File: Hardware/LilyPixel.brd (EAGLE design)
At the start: 20 x 20 mm, 11 parts, among them U1 WS2811

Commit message: Update to v10 for release
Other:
- board text added: "v10"
- board text removed: "v01"
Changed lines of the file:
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@@
 <layer number="41" name="tRestrict" color="4" fill="10" visible="no" active="yes"/>
 <layer number="42" name="bRestrict" color="1" fill="10" visible="no" active="yes"/>
+<layer number="43" name="vRestrict" color="2" fill="10" visible="no" active="yes"/>
 <layer number="44" name="Drills" color="7" fill="1" visible="no" active="yes"/>
 <layer number="45" name="Holes" color="7" fill="1" visible="yes" active="yes"/>
@@
 <layer number="37" name="tTest" color="7" fill="1" visible="no" active="no"/>
 <layer number="38" name="bTest" color="7" fill="1" visible="no" active="no"/>
-<layer number="43" name="vRestrict" color="2" fill="10" visible="no" active="no"/>
 <layer number="47" name="Measures" color="7" fill="1" visible="no" active="no"/>
 <layer number="48" name="Document" color="7" fill="1" visible="no" active="no"/>
@@
 <polygon width="0.2032" layer="29">
 <vertex x="-6" y="0"/>
-<vertex x="-11" y="0"/>
-<vertex x="-11" y="11"/>
-<vertex x="0" y="11"/>
+<vertex x="-10.111" y="0"/>
+<vertex x="-10.111" y="9.984"/>
+<vertex x="0" y="9.984"/>
 <vertex x="0" y="8.2"/>
 <vertex x="-1.4" y="7.9"/>
@@
 </polygon>
 <polygon width="0.2032" layer="29">
-<vertex x="0" y="11"/>
-<vertex x="11" y="11"/>
-<vertex x="11" y="0"/>
+<vertex x="0" y="9.984"/>
+<vertex x="10.111" y="9.984"/>
+<vertex x="10.111" y="0"/>
 <vertex x="6" y="0"/>
 <vertex x="6.7" y="0.5"/>
@@
 </polygon>
 <polygon width="0.2032" layer="29">
-<vertex x="11" y="0"/>
-<vertex x="11" y="-11"/>
-<vertex x="0" y="-11"/>
+<vertex x="10.111" y="0"/>
+<vertex x="10.111" y="-10.111"/>
+<vertex x="0" y="-10.111"/>
 <vertex x="0" y="-8.1"/>
 <vertex x="1.1" y="-8"/>
@@
 </polygon>
 <polygon width="0.2032" layer="29">
-<vertex x="0" y="-11"/>
-<vertex x="-11" y="-11"/>
-<vertex x="-11" y="0"/>
+<vertex x="0" y="-10.111"/>
+<vertex x="-10.111" y="-10.111"/>
+<vertex x="-10.111" y="0"/>
 <vertex x="-5.9" y="0"/>
 <vertex x="-6.9" y="-0.7"/>
@@
 <polygon width="0.2032" layer="41">
 <vertex x="-6" y="0"/>
-<vertex x="-11" y="0"/>
-<vertex x="-11" y="11"/>
-<vertex x="0" y="11"/>
+<vertex x="-10.111" y="0"/>
+<vertex x="-10.111" y="9.984"/>
+<vertex x="0" y="9.984"/>
 <vertex x="0" y="8.2"/>
 <vertex x="-1.4" y="7.9"/>
@@
 </polygon>
 <polygon width="0.2032" layer="41">
-<vertex x="0" y="11"/>
-<vertex x="11" y="11"/>
-<vertex x="11" y="0"/>
+<vertex x="0" y="9.984"/>
+<vertex x="10.111" y="9.984"/>
+<vertex x="10.111" y="0"/>
 <vertex x="6" y="0"/>
 <vertex x="6.7" y="0.5"/>
@@
 </polygon>
 <polygon width="0.2032" layer="41">
-<vertex x="11" y="0"/>
-<vertex x="11" y="-11"/>
-<vertex x="0" y="-11"/>
+<vertex x="10.111" y="0"/>
+<vertex x="10.111" y="-10.111"/>
+<vertex x="0" y="-10.111"/>
 <vertex x="0" y="-8.1"/>
 <vertex x="1.1" y="-8"/>
@@
 </polygon>
 <polygon width="0.2032" layer="41">
-<vertex x="0" y="-11"/>
-<vertex x="-11" y="-11"/>
-<vertex x="-11" y="0"/>
+<vertex x="0" y="-10.111"/>
+<vertex x="-10.111" y="-10.111"/>
+<vertex x="-10.111" y="0"/>
 <vertex x="-5.9" y="0"/>
 <vertex x="-6.9" y="-0.7"/>
@@
 <polygon width="0.2032" layer="42">
 <vertex x="-6" y="0"/>
-<vertex x="-11" y="0"/>
-<vertex x="-11" y="11"/>
-<vertex x="0" y="11"/>
+<vertex x="-10.111" y="0"/>
+<vertex x="-10.111" y="9.984"/>
+<vertex x="0" y="9.984"/>
 <vertex x="0" y="8.2"/>
 <vertex x="-1.4" y="7.9"/>
@@
 </polygon>
 <polygon width="0.2032" layer="42">
-<vertex x="0" y="11"/>
-<vertex x="11" y="11"/>
-<vertex x="11" y="0"/>
+<vertex x="0" y="9.984"/>
+<vertex x="10.111" y="9.984"/>
+<vertex x="10.111" y="0"/>
 <vertex x="6" y="0"/>
 <vertex x="6.7" y="0.5"/>
@@
 </polygon>
 <polygon width="0.2032" layer="42">
-<vertex x="11" y="0"/>
-<vertex x="11" y="-11"/>
-<vertex x="0" y="-11"/>
+<vertex x="10.111" y="0"/>
+<vertex x="10.111" y="-10.111"/>
+<vertex x="0" y="-10.111"/>
 <vertex x="0" y="-8.1"/>
 <vertex x="1.1" y="-8"/>
@@
 </polygon>
 <polygon width="0.2032" layer="42">
-<vertex x="0" y="-11"/>
-<vertex x="-11" y="-11"/>
-<vertex x="-11" y="0"/>
+<vertex x="0" y="-10.111"/>
+<vertex x="-10.111" y="-10.111"/>
+<vertex x="-10.111" y="0"/>
 <vertex x="-5.9" y="0"/>
 <vertex x="-6.9" y="-0.7"/>
@@
 <text x="3.81" y="1.905" size="0.8128" layer="21" font="vector" ratio="15">DI</text>
 <text x="-4.826" y="-2.667" size="0.8128" layer="21" font="vector" ratio="15">DI</text>
-<text x="-9.271" y="-1.524" size="1.27" layer="16" font="vector" ratio="15" rot="MR90">v01</text>
+<text x="-9.271" y="-1.524" size="1.27" layer="16" font="vector" ratio="15" rot="MR90">v10</text>
 </plain>
 <attributes>

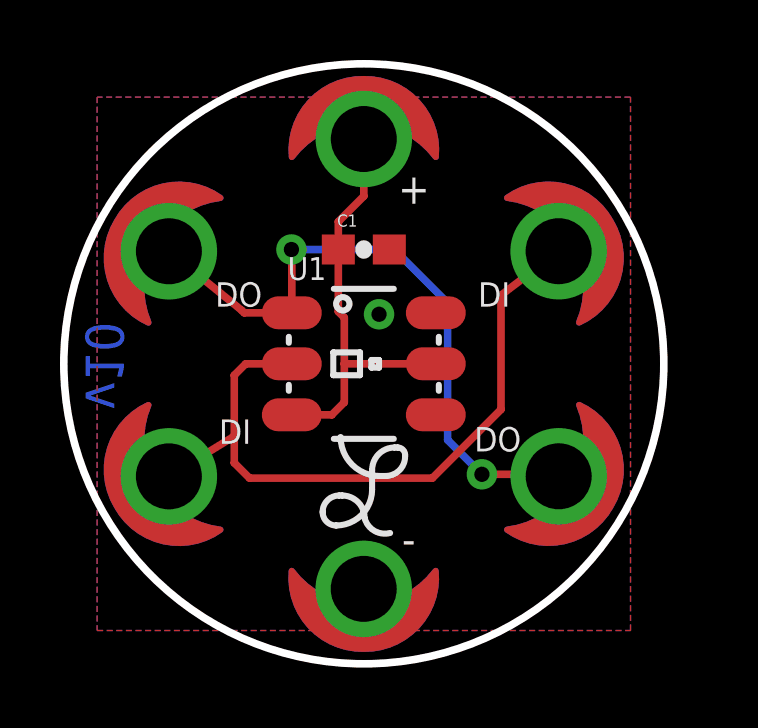
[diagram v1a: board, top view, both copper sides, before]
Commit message: replaced led package
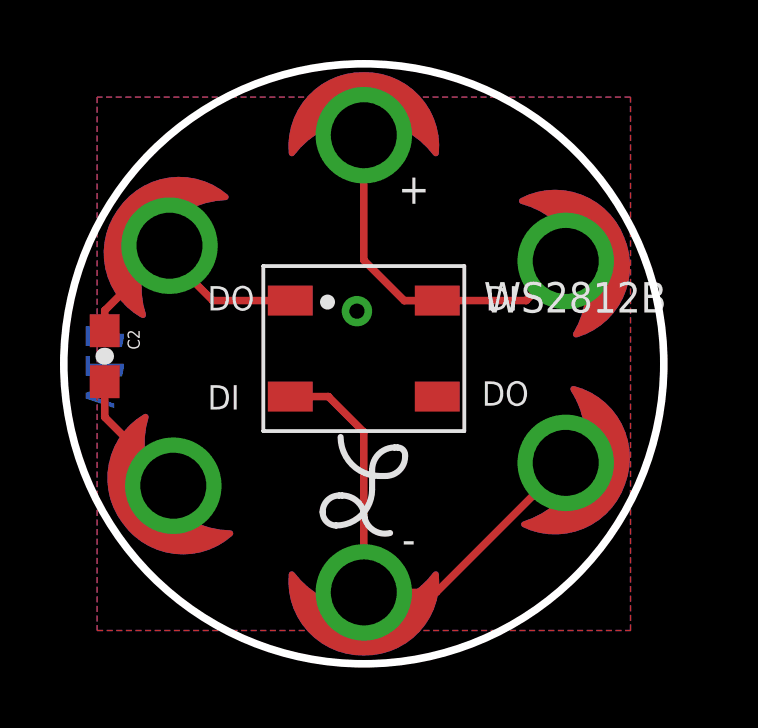
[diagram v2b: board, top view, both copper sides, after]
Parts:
- removed C1: 0.1uF, SparkFun-Capacitors:0603-CAP
- removed U$2, U$3, U$4, U$5, U$6, U$7: SEWTAP6, LilyPad-Wearables:PETAL-SMALL-2SIDE
- removed U1: WS2811, SparkFun-LED:LED-TRICOLOR-5050-IC
- added C2: 0.1uF, SparkFun-Capacitors:0603-CAP
- added LOGO1: OSHW-LOGOS, SparkFun-Aesthetics:OSHW-LOGO-S
- added U$10, U$11, U$12, U$13, U$14, U$9: SEWTAP6, LilyPad-Wearables:PETAL-SMALL-2SIDE
- added WS2812B: (no value), SparkFun-LED:WS2812B
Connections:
- removed net DI: U$2.1, U$4.1, U1.2
- removed net DO: U$3.1, U$5.1, U1.1
- new net DI1: U$10.1, U$9.1, WS2812B.4
- new net DO1: U$11.1, U$12.1, WS2812B.2
- net GND: now also C2.2, U$14.1, WS2812B.3; no longer C1.2, U$7.1, U1.6
- net VCC: now also C2.1, U$13.1, WS2812B.1; no longer C1.1, U$6.1, U1.3, U1.5
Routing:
- net DI: track 23.8 -> 0.00 mm
- net DO: track 21.7 -> 0.00 mm, vias 2 -> 0
- net DO1: track 0.00 -> 16.8 mm
- net DI1: track 0.00 -> 12.0 mm
- net VCC: track 14.2 -> 8.74 mm
- net GND: track 0.00 -> 4.41 mm
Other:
- board text added: "v11"
- board text removed: "v10"

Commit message: Fixed Shematic, full trace re route
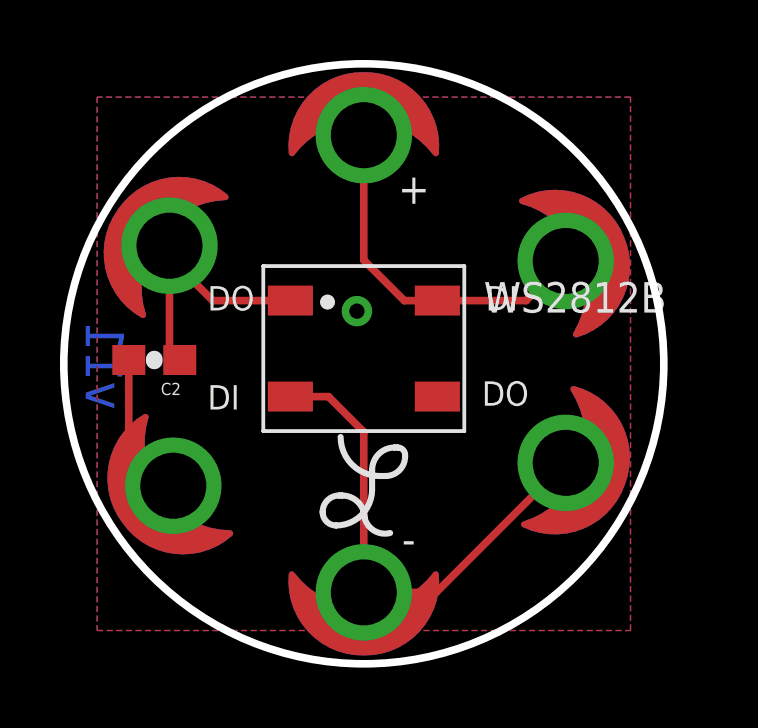
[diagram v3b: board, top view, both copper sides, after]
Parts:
- moved FRAME1 30.2 mm to (-26.7, -25.4)
- moved C2 1.66 mm to (-6.99, 0.13), turned to 180 degrees
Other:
- board text added: "Mike Hord"
- board text added: "Revised by: Patrick Alberts"
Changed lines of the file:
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@@
 <setting verticaltext="up"/>
 </settings>
-<grid distance="0.05" unitdist="inch" unit="inch" style="lines" multiple="1" display="yes" altdistance="0.0001" altunitdist="inch" altunit="inch"/>
+<grid distance="0.05" unitdist="inch" unit="inch" style="lines" multiple="1" display="yes" altdistance="0.005" altunitdist="inch" altunit="inch"/>
 <layers>
 <layer number="1" name="Top" color="4" fill="1" visible="yes" active="yes"/>
@@
 <text x="-5.207" y="-1.524" size="0.8128" layer="21" font="vector" ratio="15">DI</text>
 <text x="-9.271" y="-1.524" size="1.27" layer="16" font="vector" ratio="15" rot="MR90">v11</text>
+<text x="3.81" y="-25.4" size="1.778" layer="51" font="vector" ratio="10">Mike Hord</text>
+<text x="-15.24" y="-27.94" size="1.778" layer="51" font="vector" ratio="10">Revised by: Patrick Alberts</text>
 </plain>
 <attributes>
@@
 <elements>
 <element name="U$8" library="LilyPad-Wearables" package="LOGO-L" value="LOGO-LPL" x="0" y="-4.064"/>
-<element name="FRAME1" library="SparkFun-Aesthetics" package="CREATIVE_COMMONS" value="FRAME-LETTER" x="2.54" y="-33.02"/>
+<element name="FRAME1" library="SparkFun-Aesthetics" package="CREATIVE_COMMONS" value="FRAME-LETTER" x="-26.67" y="-25.4"/>
 <element name="U$1" library="LilyPad-Wearables" package="LOGO-LILYPAD" value="LOGO-LPLP" x="0" y="0" rot="MR0"/>
 <element name="WS2812B" library="SparkFun-LED" package="WS2812B" value="" x="0" y="0.508"/>
@@
 <element name="U$12" library="LilyPad-Wearables" package="PETAL-SMALL-2SIDE" value="SEWTAP6" x="6.731" y="-3.302" rot="R70"/>
 <element name="U$13" library="LilyPad-Wearables" package="PETAL-SMALL-2SIDE" value="SEWTAP6" x="-6.477" y="3.937" rot="R235"/>
-<element name="C2" library="SparkFun-Capacitors" package="0603-CAP" value="0.1uF" x="-8.636" y="0.254" rot="R270">
-<attribute name="PROD_ID" value="CAP-00810" x="-8.636" y="0.254" size="1.778" layer="27" font="vector" ratio="15" rot="R270" display="off"/>
+<element name="C2" library="SparkFun-Capacitors" package="0603-CAP" value="0.1uF" x="-6.985" y="0.127" rot="R180">
+<attribute name="PROD_ID" value="CAP-00810" x="-6.985" y="0.127" size="1.778" layer="27" font="vector" ratio="15" rot="R180" display="off"/>
 </element>
 <element name="U$14" library="LilyPad-Wearables" package="PETAL-SMALL-2SIDE" value="SEWTAP6" x="-6.35" y="-4.064" rot="R306"/>
@@
 <wire x1="-5.03681875" y1="2.1082" x2="-2.4502" y2="2.1082" width="0.254" layer="1"/>
 <wire x1="-2.4502" y1="2.1082" x2="-2.45" y2="2.108" width="0.254" layer="1"/>
-<wire x1="-8.636" y1="1.104" x2="-8.636" y2="1.778" width="0.254" layer="1"/>
-<wire x1="-8.636" y1="1.778" x2="-6.477" y2="3.937" width="0.254" layer="1"/>
+<wire x1="-6.135" y1="0.127" x2="-6.477" y2="0.469" width="0.254" layer="1"/>
+<wire x1="-6.477" y1="0.469" x2="-6.477" y2="3.937" width="0.254" layer="1"/>
 </signal>
 <signal name="GND">
@@
 <contactref element="WS2812B" pad="3"/>
 <contactref element="U$14" pad="1"/>
-<wire x1="-8.636" y1="-0.596" x2="-8.636" y2="-1.778" width="0.254" layer="1"/>
-<wire x1="-8.636" y1="-1.778" x2="-6.35" y2="-4.064" width="0.254" layer="1"/>
+<wire x1="-6.35" y1="-4.064" x2="-7.835" y2="-2.579" width="0.254" layer="1"/>
+<wire x1="-7.835" y1="-2.579" x2="-7.835" y2="0.127" width="0.254" layer="1"/>
 </signal>
 <signal name="N$7">

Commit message: Trace Cleanup
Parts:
- moved C2 2.55 mm to (-4.45, 0.38), turned to 90 degrees
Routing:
- net GND: track 4.81 -> 0.00 mm
- net VCC: track 8.96 -> 10.0 mm
- net DO1: track 16.8 -> 17.6 mm
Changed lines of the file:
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@@
 <vertex x="0" y="-8.2"/>
 </polygon>
-<text x="-5.207" y="1.778" size="0.8128" layer="21" font="vector" ratio="15">DO</text>
-<text x="3.937" y="-1.397" size="0.8128" layer="21" font="vector" ratio="15">DO</text>
-<text x="4.064" y="1.778" size="0.8128" layer="21" font="vector" ratio="15">DI</text>
-<text x="-5.207" y="-1.524" size="0.8128" layer="21" font="vector" ratio="15">DI</text>
-<text x="-9.271" y="-1.524" size="1.27" layer="16" font="vector" ratio="15" rot="MR90">v11</text>
+<text x="-4.826" y="2.413" size="0.8128" layer="21" font="vector" ratio="15">DO</text>
+<text x="3.556" y="-2.159" size="0.8128" layer="21" font="vector" ratio="15">DO</text>
+<text x="3.556" y="2.413" size="0.8128" layer="21" font="vector" ratio="15">DI</text>
+<text x="-4.699" y="-2.159" size="0.8128" layer="21" font="vector" ratio="15">DI</text>
+<text x="4.318" y="3.683" size="0.8128" layer="16" font="vector" ratio="15" rot="MR0">v11</text>
 <text x="3.81" y="-25.4" size="1.778" layer="51" font="vector" ratio="10">Mike Hord</text>
 <text x="-15.24" y="-27.94" size="1.778" layer="51" font="vector" ratio="10">Revised by: Patrick Alberts</text>
@@
 <element name="U$12" library="LilyPad-Wearables" package="PETAL-SMALL-2SIDE" value="SEWTAP6" x="6.731" y="-3.302" rot="R70"/>
 <element name="U$13" library="LilyPad-Wearables" package="PETAL-SMALL-2SIDE" value="SEWTAP6" x="-6.477" y="3.937" rot="R235"/>
-<element name="C2" library="SparkFun-Capacitors" package="0603-CAP" value="0.1uF" x="-6.985" y="0.127" rot="R180">
-<attribute name="PROD_ID" value="CAP-00810" x="-6.985" y="0.127" size="1.778" layer="27" font="vector" ratio="15" rot="R180" display="off"/>
+<element name="C2" library="SparkFun-Capacitors" package="0603-CAP" value="0.1uF" x="-4.445" y="0.381" rot="R90">
+<attribute name="PROD_ID" value="CAP-00810" x="-4.445" y="0.381" size="1.778" layer="27" font="vector" ratio="15" rot="R90" display="off"/>
 </element>
 <element name="U$14" library="LilyPad-Wearables" package="PETAL-SMALL-2SIDE" value="SEWTAP6" x="-6.35" y="-4.064" rot="R306"/>
@@
 <contactref element="C2" pad="1"/>
 <contactref element="WS2812B" pad="1"/>
-<wire x1="-6.477" y1="3.937" x2="-6.477" y2="3.54838125" width="0.254" layer="1"/>
-<wire x1="-6.477" y1="3.54838125" x2="-5.03681875" y2="2.1082" width="0.254" layer="1"/>
-<wire x1="-5.03681875" y1="2.1082" x2="-2.4502" y2="2.1082" width="0.254" layer="1"/>
 <wire x1="-2.4502" y1="2.1082" x2="-2.45" y2="2.108" width="0.254" layer="1"/>
-<wire x1="-6.135" y1="0.127" x2="-6.477" y2="0.469" width="0.254" layer="1"/>
-<wire x1="-6.477" y1="0.469" x2="-6.477" y2="3.937" width="0.254" layer="1"/>
+<wire x1="-2.4502" y1="2.1082" x2="-3.5052" y2="2.1082" width="0.254" layer="1"/>
+<wire x1="-3.5052" y1="2.1082" x2="-5.334" y2="3.937" width="0.254" layer="1"/>
+<wire x1="-5.334" y1="3.937" x2="-6.477" y2="3.937" width="0.254" layer="1"/>
+<wire x1="-6.477" y1="3.937" x2="-6.477" y2="1.563" width="0.254" layer="1"/>
+<wire x1="-6.477" y1="1.563" x2="-4.445" y2="-0.469" width="0.254" layer="1"/>
 </signal>
 <signal name="GND">
@@
 <contactref element="WS2812B" pad="3"/>
 <contactref element="U$14" pad="1"/>
-<wire x1="-6.35" y1="-4.064" x2="-7.835" y2="-2.579" width="0.254" layer="1"/>
-<wire x1="-7.835" y1="-2.579" x2="-7.835" y2="0.127" width="0.254" layer="1"/>
 </signal>
 <signal name="N$7">
@@
 <contactref element="U$11" pad="1"/>
 <contactref element="WS2812B" pad="2"/>
-<wire x1="0" y1="-7.62" x2="2.413" y2="-7.62" width="0.254" layer="1"/>
-<wire x1="2.413" y1="-7.62" x2="6.731" y2="-3.302" width="0.254" layer="1"/>
 <wire x1="0" y1="-7.62" x2="0" y2="-2.270759375" width="0.254" layer="1"/>
 <wire x1="0" y1="-2.270759375" x2="-1.178559375" y2="-1.0922" width="0.254" layer="1"/>
 <wire x1="-1.178559375" y1="-1.0922" x2="-2.4498" y2="-1.0922" width="0.254" layer="1"/>
 <wire x1="-2.4498" y1="-1.0922" x2="-2.45" y2="-1.092" width="0.254" layer="1"/>
+<wire x1="0" y1="-7.62" x2="1.27" y2="-6.35" width="0.254" layer="1"/>
+<wire x1="1.27" y1="-6.35" x2="1.27" y2="-5.08" width="0.254" layer="1"/>
+<wire x1="1.27" y1="-5.08" x2="3.048" y2="-3.302" width="0.254" layer="1"/>
+<wire x1="3.048" y1="-3.302" x2="6.731" y2="-3.302" width="0.254" layer="1"/>
 </signal>
 </signals>
